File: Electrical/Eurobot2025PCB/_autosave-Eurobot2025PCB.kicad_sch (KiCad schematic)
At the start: 24 parts, among them J1 Screw_Terminal_01x02, J2 Conn_01x04_Socket, J3 Conn_01x04_Socket, J4 Conn_01x04_Socket, J5 Screw_Terminal_01x02, M1 Motor_Servo, M2 Motor_Servo, M3 Motor_Servo, SW1 SW_SPDT, SW2 SW_SPDT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

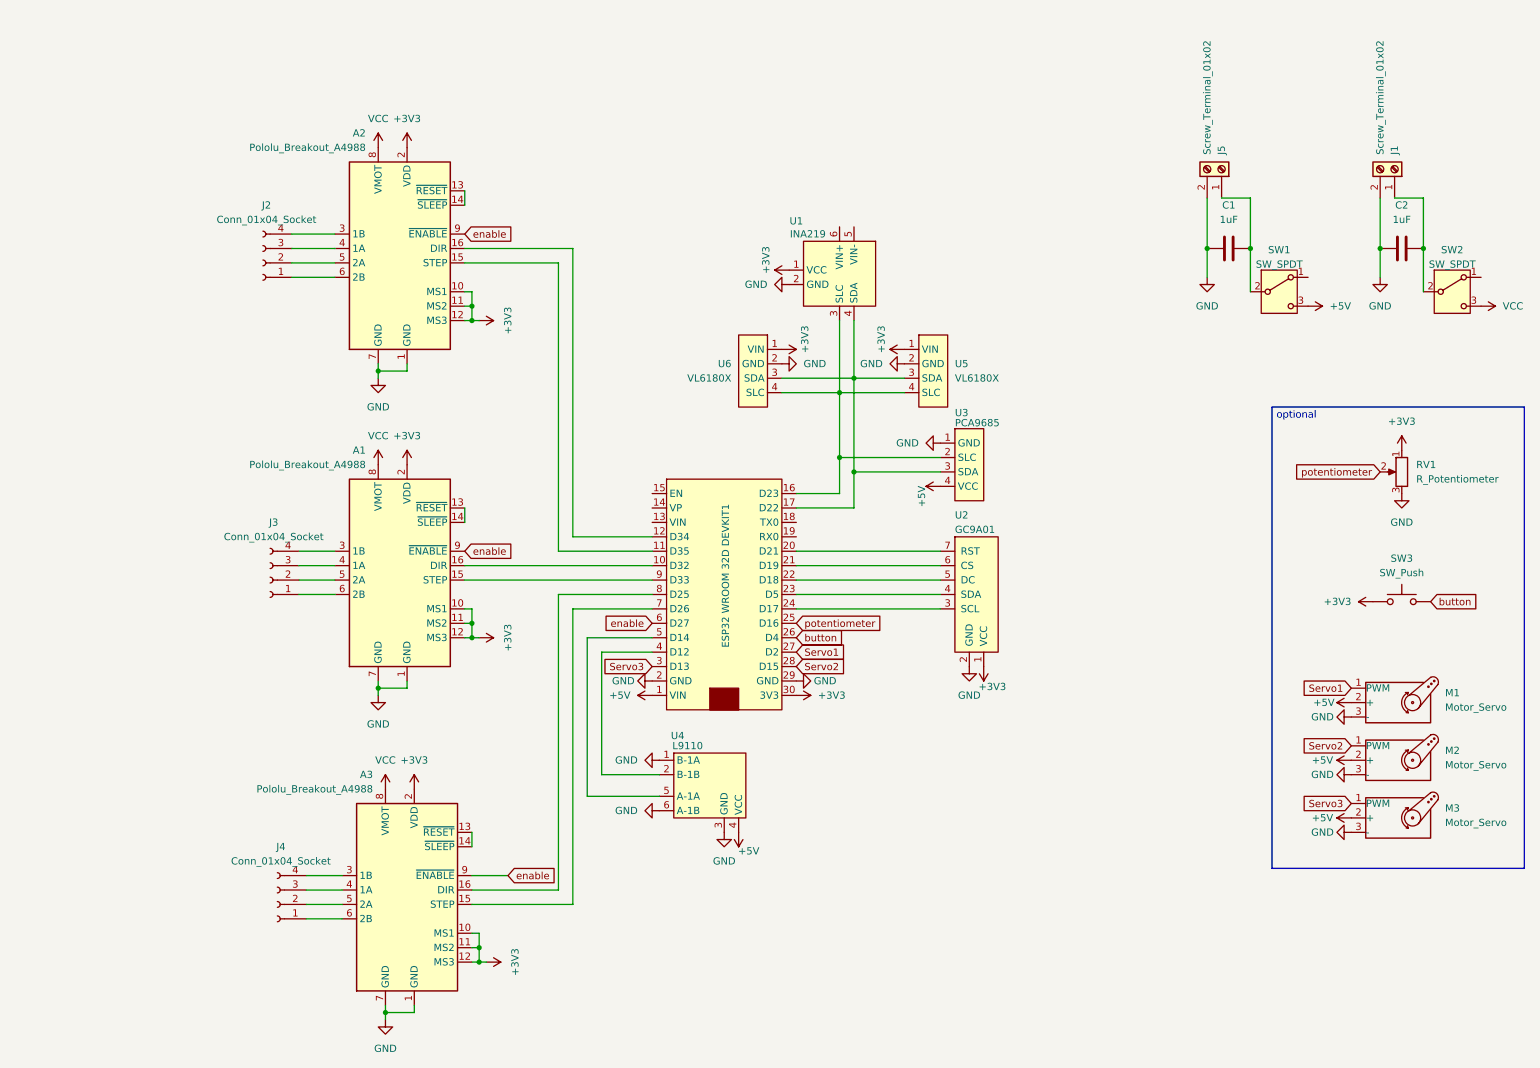
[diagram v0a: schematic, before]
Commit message: Add 4th step motor and 12V to 5V converter to PCB
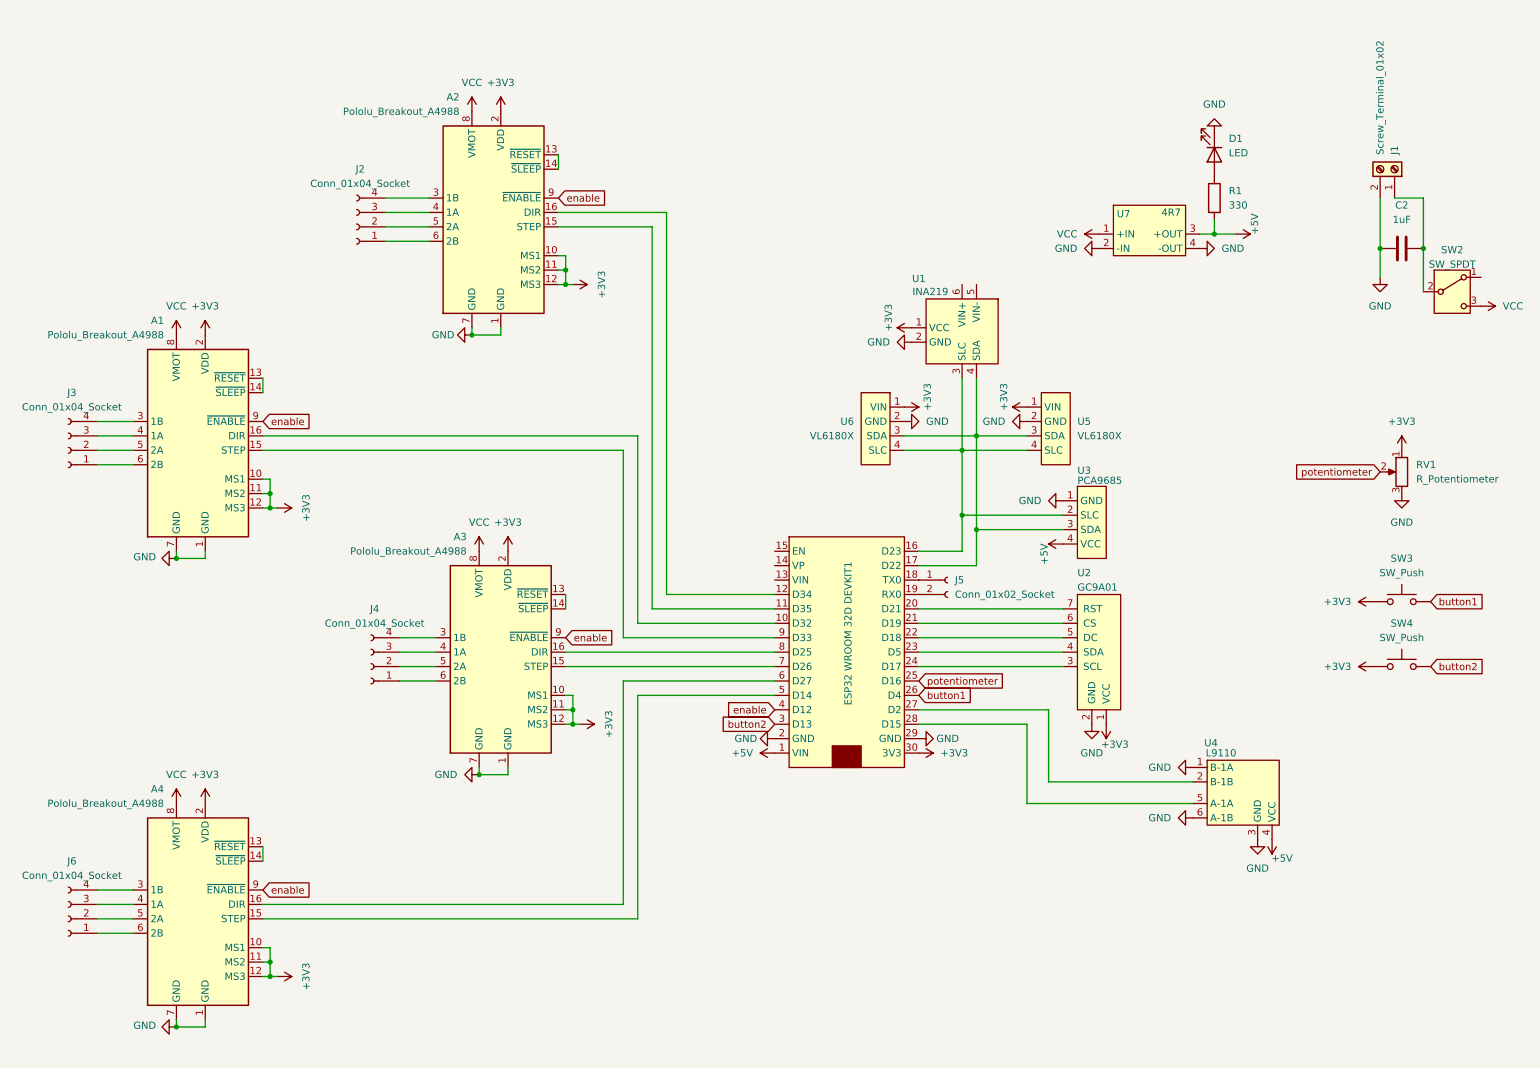
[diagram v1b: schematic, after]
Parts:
- removed C1: 1uF, Capacitor_THT:C_Radial_D5.0mm_H11.0mm_P2.00mm, symbol Device:C
- removed J5: Screw_Terminal_01x02, TerminalBlock_MetzConnect:TerminalBlock_MetzConnect_Type059_RT06302HBWC_1x02_P3.50mm_Horizontal, symbol Connector:Screw_Terminal_01x02
- removed M1, M2, M3: Motor_Servo, Connector_PinHeader_2.54mm:PinHeader_1x03_P2.54mm_Vertical, symbol Motor:Motor_Servo
- removed SW1: SW_SPDT, Button_Switch_THT:SW_XKB_DM1-16UP-1, symbol Switch:SW_SPDT
- added A4: Pololu_Breakout_A4988, ECN:A4988, symbol Driver_Motor:Pololu_Breakout_A4988
- added D1: LED, LED_THT:LED_D5.0mm, symbol Device:LED
- added J5: Conn_01x02_Socket, Connector_PinHeader_2.54mm:PinHeader_1x02_P2.54mm_Vertical, symbol Connector:Conn_01x02_Socket
- added J6: Conn_01x04_Socket, Connector_JST:JST_XH_B4B-XH-A_1x04_P2.50mm_Vertical, symbol Connector:Conn_01x04_Socket
- added R1: 330, Resistor_THT:R_Axial_DIN0207_L6.3mm_D2.5mm_P10.16mm_Horizontal, symbol Device:R
- added SW4: SW_Push, Button_Switch_THT:SW_PUSH_6mm, symbol Switch:SW_Push
- added U7: 4R7, ECN:4R7, symbol ECN:4R7
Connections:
- net Servo1 is gone; now on an unnamed net: ESP32 WROOM 32D DEVKIT1.27 (D2)
- net +3V3: now also A4.10 (MS1), A4.11 (MS2), A4.12 (MS3), A4.2 (VDD), SW4.1
- net +5V: now also R1.2, U7.3 (+OUT)
- net GND: now also A4.1 (GND), A4.7 (GND), D1.1 (K), U7.2 (-IN), U7.4 (-OUT)
- net VCC: now also A4.8 (VMOT), U7.1 (+IN)
- net enable: now also ESP32 WROOM 32D DEVKIT1.4 (D12), A4.9 (~{ENABLE}); no longer ESP32 WROOM 32D DEVKIT1.6 (D27)
- net at ESP32 WROOM 32D DEVKIT1.18 (TX0): now also J5.1 (Pin_1)
- net at ESP32 WROOM 32D DEVKIT1.19 (RX0): now also J5.2 (Pin_2)
- net at U4.2 (B-1B): no longer ESP32 WROOM 32D DEVKIT1.4 (D12)
- net at ESP32 WROOM 32D DEVKIT1.5 (D14): now also A4.15 (STEP); no longer U4.5 (A-1A)
- net Servo2: no longer names the net of ESP32 WROOM 32D DEVKIT1.28 (D15)
- net Servo2: now also U4.5 (A-1A)
- net Servo3 renamed button2
- net button2: now also SW4.2
- net button renamed button1
- new net: A4.6 (2B), J6.1 (Pin_1)
- new net: A4.5 (2A), J6.2 (Pin_2)
- new net: A4.4 (1A), J6.3 (Pin_3)
- new net: A4.3 (1B), J6.4 (Pin_4)
- new net: A4.13 (~{RESET}), A4.14 (~{SLEEP})
- new net: A4.16 (DIR), ESP32 WROOM 32D DEVKIT1.6 (D27)
- new net: D1.2 (A), R1.1
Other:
- note removed: "optional"
- moved on the sheet: A1, A2, A3, ESP32 WROOM 32D DEVKIT1, J2, J3, J4, U1, U2, U3, U4, U5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
